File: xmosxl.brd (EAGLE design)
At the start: 130 x 85 mm, 106 parts, among them IC1 74LVC1T45W6-7, IC2 74LVC1T45W6-7, IC3 74LVC1T45W6-7, IC4 74LVC1T45W6-7, IC5 74LVC1T45W6-7, IC6 74ALVC164245DGG_11, IC7 74ALVC164245DGG_11, IC8 74LVC1T45W6-7, IC9 74LVC1T45W6-7, U1 24 MHz Osc. (F535L-24)

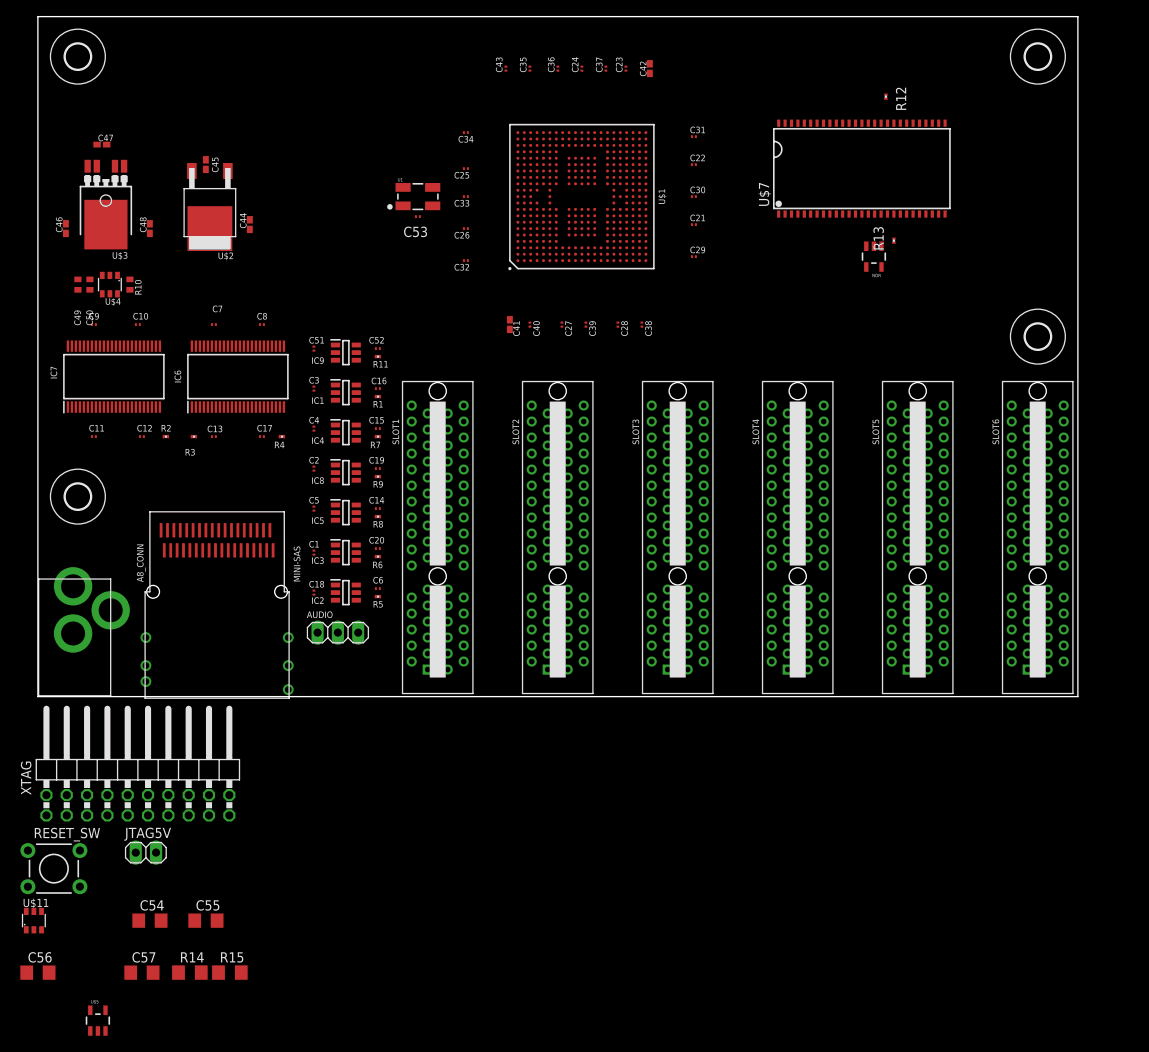
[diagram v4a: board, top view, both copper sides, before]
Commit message: Remove a slot - left with 5. Can add an “expansion box” for the remaining 5.
Add the JTAG link.
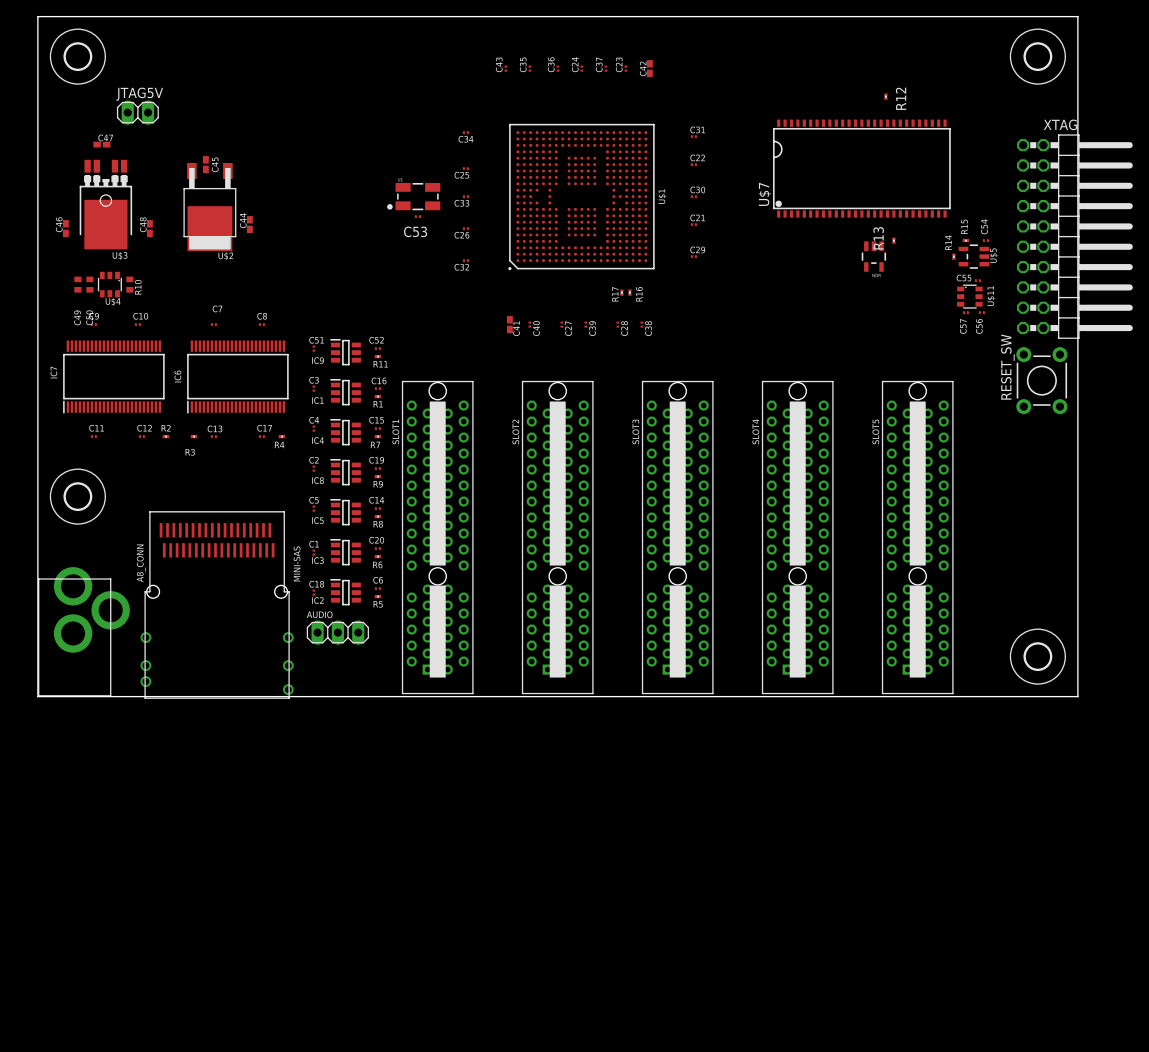
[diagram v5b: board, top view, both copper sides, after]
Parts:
- removed SLOT6: PCIE_64, pcie:PCI-E_64
- added R16, R17: 33R, rcl:R0201
- C54, C55: value 100nF -> 0.1uF; device rcl:C1206 -> rcl:C0201
- C56, C57: device rcl:C1206 -> rcl:C0201
- R14, R15: device rcl:R1206 -> rcl:R0201
- moved U$5 145.3 mm to (117.0, 55.0), turned to 90 degrees
- moved C56 144.0 mm to (118.0, 48.0)
- moved U$11 140.6 mm to (116.5, 50.0), turned to 270 degrees
- moved RESET_SW 137.7 mm to (125.5, 39.5), turned to 90 degrees
- moved C54 134.7 mm to (118.5, 57.0), turned to 180 degrees
- moved XTAG 134.3 mm to (129.5, 57.5), turned to 270 degrees
- moved C57 132.0 mm to (116.0, 48.0), turned to 180 degrees
- moved R14 130.9 mm to (114.5, 55.0), turned to 270 degrees
- moved R15 129.8 mm to (116.0, 57.0)
- moved C55 125.3 mm to (117.5, 52.0), turned to 180 degrees
- moved JTAG5V 92.5 mm to (12.5, 73.0)
- moved H4 40.0 mm to (125.0, 5.00)
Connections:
- removed net N$4: C55.1, R15.2, U$11.6
- removed net N$7: C54.1
- new net N$22: R16.1, U$1.V2
- new net N$23: R17.1, U$1.V1
- net +3V3: now also C54.1, C55.1, R15.2, U$11.6
- net JTAG_DN0: now also U$1.U1
- net JTAG_DN1: now also U$1.U2
- net JTAG_UP0: now also R16.2
- net JTAG_UP1: now also R17.2

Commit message: Start work on the slots
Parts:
- added C58: 0.1uF, rcl:C0201
- added DBG0, DBG1, DBG2, DBG3: ok33, led:CHIP-LED0603
- added R18, R19, R22, R23, R25, R26: 10K, rcl:R0201
- added R20, R21, R55, R56: 1K, rcl:R0201
- added R24: 2.2R, rcl:R0201
- moved C26 0.75 mm to (53.5, 57.8)
- renumbered U$1 to XMOS
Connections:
- new net !DEBUG!: XMOS.D9, XTAG.11
- new net N$10: R26.2, XMOS.D10
- new net N$16: DBG0.C, R21.2
- new net N$18: DBG3.C, R55.2
- new net N$19: DBG1.C, R20.2
- new net N$3: DBG2.C, R56.2
- new net N$4: DBG0.A, XMOS.C16
- new net N$56: DBG1.A, XMOS.D16
- new net N$57: DBG2.A, XMOS.C17
- new net N$63: DBG3.A, XMOS.D17
- new net N$7: C58.1, R24.2, XMOS.F11
- new net N$9: R25.1, XMOS.C10
- new net SBUS_A0: XMOS.A5
- new net SBUS_A1: XMOS.B5
- new net SBUS_A10: XMOS.T1
- new net SBUS_A11: XMOS.U3
- new net SBUS_A12: XMOS.B7
- new net SBUS_A13: XMOS.A7
- new net SBUS_A14: XMOS.B6
- new net SBUS_A15: XMOS.C6
- new net SBUS_A2: XMOS.C5
- new net SBUS_A3: XMOS.D5
- new net SBUS_A4: XMOS.C4
- new net SBUS_A5: XMOS.D4
- new net SBUS_A6: XMOS.A4
- new net SBUS_A7: XMOS.B4
- new net SBUS_A8: XMOS.F1
- new net SBUS_A9: XMOS.R3
- new net SBUS_CLK: XMOS.AA8
- new net SBUS_D0: XMOS.G1
- new net SBUS_D1: XMOS.G2
- new net SBUS_D2: XMOS.G3
- new net SBUS_D3: XMOS.H2
- new net SBUS_D4: XMOS.H1
- new net SBUS_D5: XMOS.J1
- new net SBUS_D6: XMOS.J2
- new net SBUS_D7: XMOS.K3
- new net SBUS_FLG0: XMOS.K2
- new net SBUS_FLG1: XMOS.K1
- new net SBUS_FLG2: XMOS.V8
- new net SBUS_FLG3: XMOS.W8
- new net SBUS_FLG4: XMOS.Y8
- new net SPI_BOPT0: XMOS.W9
- new net SPI_BOPT1: XMOS.Y9
- new net SPI_BOPT2: XMOS.AA9
- new net SPI_BOPT3: XMOS.V10
- new net SPI_BSEL0: XMOS.V4
- new net SPI_BSEL1: XMOS.W4
- new net SPI_BSEL2: XMOS.V5
- new net SPI_BSEL3: XMOS.W5
- new net SPI_CLK0: XMOS.Y2
- new net SPI_CLK1: XMOS.W2
- new net SPI_IRQ0: XMOS.B9
- new net SPI_IRQ1: XMOS.A9
- new net SPI_IRQ2: XMOS.B8
- new net SPI_IRQ3: XMOS.A8
- new net SPI_IRQ4: XMOS.C9
- new net SPI_IRQ5: XMOS.C8
- new net SPI_IRQ6: XMOS.D2
- new net SPI_IRQ7: XMOS.D1
- new net SPI_IRQ8: XMOS.E2
- new net SPI_IRQ9: XMOS.E1
- new net SPI_MISO0: XMOS.V6
- new net SPI_MISO1: XMOS.Y1
- new net SPI_MOSI0: XMOS.W10
- new net SPI_MOSI1: XMOS.Y7
- new net SPI_SS0: XMOS.Y10
- new net SPI_SS1: XMOS.AA10
- new net SPI_SS2: XMOS.W11
- new net SPI_SS3: XMOS.B2
- new net SPI_SS4: XMOS.B1
- new net SPI_SS5: XMOS.C2
- new net SPI_SS6: XMOS.C1
- new net SPI_SS7: XMOS.Y5
- new net SPI_SS8: XMOS.AA5
- new net SPI_SS9: XMOS.V9
- net !EXTSEL!: now also XMOS.D21
- net !EXTSEL!_DIR: now also XMOS.B14
- net !HALT!: now also XMOS.B10
- net !HALT!_DIR: now also XMOS.C14
- net !IRQ!: now also XMOS.B21
- net !IRQ!_DIR: now also XMOS.D14
- net !MPD!: now also XMOS.C20
- net !MPD!_DIR: now also XMOS.AA19
- net !REF!: now also XMOS.V12
- net !REF!_DIR: now also XMOS.A15
- net !RESET!: now also XMOS.B12, XMOS.C12
- net !RST!: now also XMOS.C21
- net !RST!_DIR: now also XMOS.B16
- net +3V3: now also R18.1, R25.2, XMOS.C11
- net A0: now also XMOS.R19
- net A1: now also XMOS.N20
- net A10: now also XMOS.J21
- net A11: now also XMOS.J20
- net A12: now also XMOS.H20
- net A13: now also XMOS.H21
- net A14: now also XMOS.G21
- net A15: now also XMOS.G20
- net A2: now also XMOS.N21
- net A3: now also XMOS.M21
- net A4: now also XMOS.M20
- net A5: now also XMOS.M19
- net A6: now also XMOS.L19
- net A7: now also XMOS.K19
- net A8: now also XMOS.K20
- net A9: now also XMOS.K21
- net A_DIR: now also XMOS.B15
- net CLK: now also XMOS.Y21
- net D0: now also XMOS.B20
- net D1: now also XMOS.B19
- net D2: now also XMOS.B18
- net D3: now also XMOS.A18
- net D4: now also XMOS.B17
- net D5: now also XMOS.A17
- net D6: now also XMOS.A19
- net D7: now also XMOS.C18
- net D_DIR: now also XMOS.A14
- net GND: now also C58.2, R19.1, R20.1, R21.1, R22.1, R23.1, R26.1, R55.1, R56.1, XMOS.D18, XMOS.E19, XMOS.F10, XMOS.F21, XMOS.G19, XMOS.V17, XMOS.W17
- net R/!W!: now also XMOS.W20
- net R/!W!_DIR: now also XMOS.D15
- net RD4: now also XMOS.W18
- net RD5: now also XMOS.V18
- net SD_ADQ1: now also R19.2
- net SD_ADQ2: now also R22.2
- net SD_ADQ3: now also R18.2
- net SD_ADQ7: now also R23.2
- net VDD: now also R24.1

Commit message: Add the links
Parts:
- added C59, C60, C61, C62, C63, C64, C65, C66: 100nF, rcl:C0201
- added I2C0, I2C1: (no value), pinhead:1X02
- added JP1: (no value), pinhead:2X09
- added R27, R28: 43R2, rcl:R0201
- added R29, R30: 4K7, rcl:R0201
- added R31, R32, R33, R34, R35: 33R, rcl:R0201
- added UART: (no value), pinhead:1X03
- moved JTAG5V 21.7 mm to (3.00, 53.5), turned to 270 degrees
- moved DBG0 5.00 mm to (51.0, 81.0)
- moved DBG1 5.00 mm to (53.8, 81.0)
- moved DBG2 5.00 mm to (56.5, 81.0)
- moved DBG3 5.00 mm to (59.2, 81.0)
- moved R20 5.00 mm to (53.8, 83.0)
- moved R21 5.00 mm to (51.0, 83.0)
- moved R55 5.00 mm to (59.2, 83.0)
- moved R56 5.00 mm to (56.5, 83.0)
- moved C49 4.00 mm to (9.00, 51.5)
- moved C50 4.00 mm to (10.5, 51.5)
- moved R10 4.00 mm to (15.5, 51.5)
- moved U$4 4.00 mm to (13.0, 51.5)
- moved XTAG 2.00 mm to (129.5, 59.5)
- moved RESET_SW 1.50 mm to (125.5, 41.0)
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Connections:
- new net N$11: R27.2, XMOS.W16
- new net N$12: R28.2, XMOS.W6
- new net N$13: UART.2, XMOS.E3
- new net N$20: UART.1, XMOS.D3
- new net N$21: JP1.4
- new net N$24: JP1.8
- new net N$25: JP1.12
- new net N$26: JP1.16
- new net N$27: R31.1, XMOS.N2
- new net N$28: R32.1, XMOS.P2
- new net N$29: R34.1, XMOS.R1
- new net N$30: R35.1, XMOS.R2
- new net RX0: JP1.1, XMOS.N1
- new net RX1: JP1.5, XMOS.M1
- new net RX2: JP1.9, XMOS.M2
- new net RX3: JP1.13, XMOS.M3
- new net RX4: JP1.17, R33.1, XMOS.L3, XMOS.P1
- new net SCL: I2C0.1, I2C1.1, R29.1, XMOS.A3
- new net SDA: I2C0.2, I2C1.2, R30.1, XMOS.B3
- new net TX0: JP1.2, R31.2
- new net TX1: JP1.6, R32.2
- new net TX2: JP1.10, R33.2
- new net TX3: JP1.14, R34.2
- new net TX4: JP1.18, R35.2
- net +3V3: now also C59.1, C60.1, C61.1, C62.1, C63.1, C64.1, C65.1, C66.1, JP1.11, R29.2, R30.2
- net +5V: now also JP1.7
- net GND: now also C59.2, C60.2, C61.2, C62.2, C63.2, C64.2, C65.2, C66.2, JP1.3, R27.1, R28.1, UART.3
- net VDD: now also JP1.15
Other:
- board text added: "+"
- board text added: "Gnd"
- board text added: "Rx"
- board text added: "SCL"
- board text added: "SDA"
- board text added: "Tx"
